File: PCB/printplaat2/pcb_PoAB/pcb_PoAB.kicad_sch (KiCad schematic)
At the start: 28 parts, among them J1 battertij, J2 lichtmeter1, J3 lichtmeter2, J4 lichtmeter3, J5 lichtmeter4, J6 lamp1, J7 lamp2, J8 lamp3, J9 spannigsmeter, U1 L7805CV, U2 AQY211EHAZ, U3 AQY211EHAZ, U4 AQY211EHAZ, U5 ACS712ELCTR-05B-T, U6 ACS712ELCTR-05B-T, U7 ACS712ELCTR-05B-T, U9 ARDUINO_MKR_WAN_1310

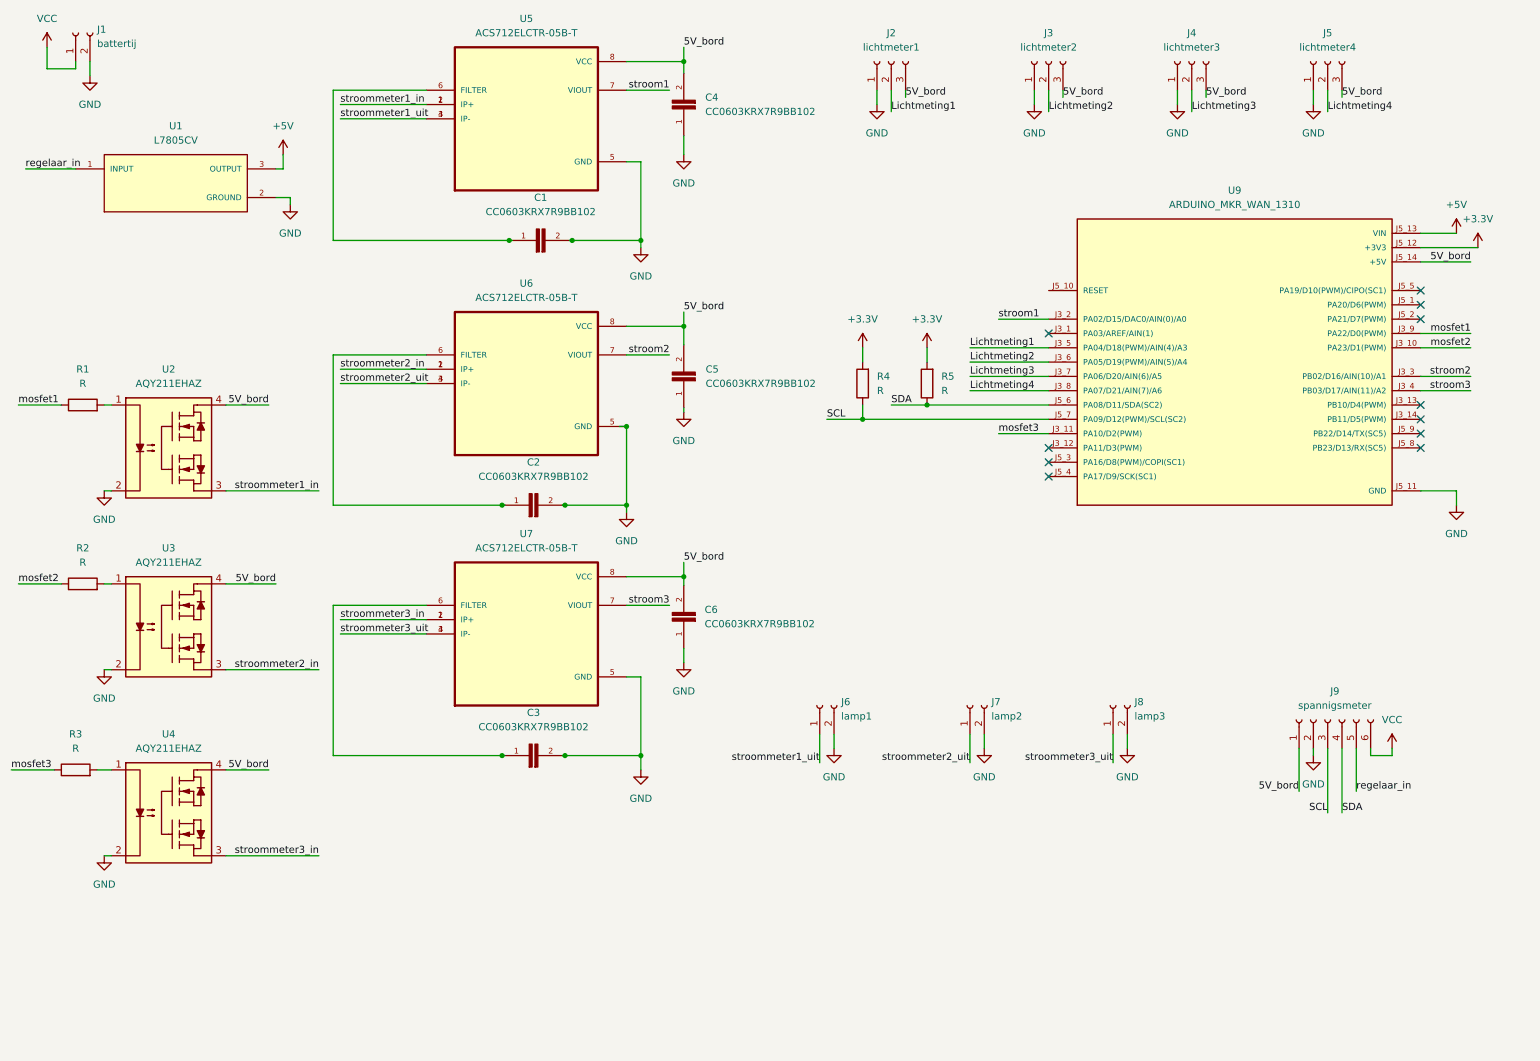
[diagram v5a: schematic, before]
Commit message: PCB en schema spanning en stroommetingen aangepast
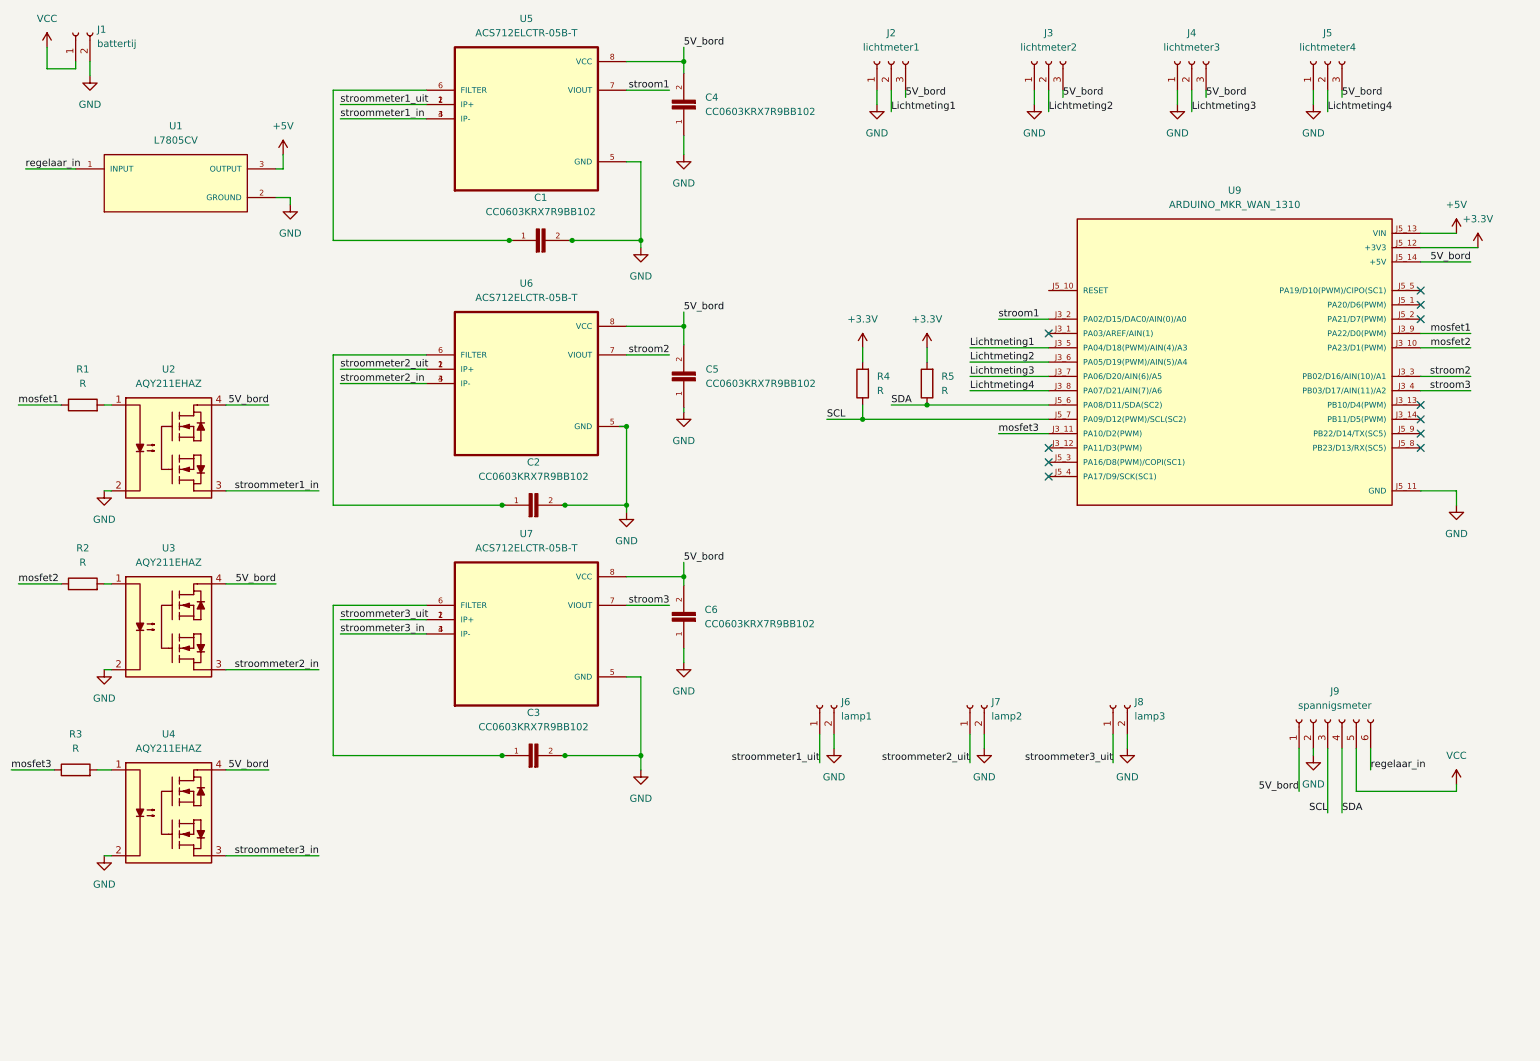
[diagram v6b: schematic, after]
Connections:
- net VCC: now also J9.5 (Pin_5); no longer J9.6 (Pin_6)
- net regelaar_in: now also J9.6 (Pin_6); no longer J9.5 (Pin_5)
- net stroommeter1_in: now also U5.3 (IP-), U5.4 (IP-); no longer U5.1 (IP+), U5.2 (IP+)
- net stroommeter1_uit: now also U5.1 (IP+), U5.2 (IP+); no longer U5.3 (IP-), U5.4 (IP-)
- net stroommeter2_in: now also U6.3 (IP-), U6.4 (IP-); no longer U6.1 (IP+), U6.2 (IP+)
- net stroommeter2_uit: now also U6.1 (IP+), U6.2 (IP+); no longer U6.3 (IP-), U6.4 (IP-)
- net stroommeter3_in: now also U7.3 (IP-), U7.4 (IP-); no longer U7.1 (IP+), U7.2 (IP+)
- net stroommeter3_uit: now also U7.1 (IP+), U7.2 (IP+); no longer U7.3 (IP-), U7.4 (IP-)
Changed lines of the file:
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@@
     (stroke (width 0) (type default) (color 0 0 0 0))
   )
-  (wire (pts (xy 255.27 144.78) (xy 255.27 143.51))
+  (wire (pts (xy 255.27 147.32) (xy 255.27 143.51))
     (stroke (width 0) (type default) (color 0 0 0 0))
   )
@@
     (stroke (width 0) (type default) (color 0 0 0 0))
   )
-  (wire (pts (xy 259.08 143.51) (xy 259.08 144.78))
+  (wire (pts (xy 252.73 151.13) (xy 270.51 151.13))
     (stroke (width 0) (type default) (color 0 0 0 0))
   )
@@
     (stroke (width 0) (type default) (color 0 0 0 0))
   )
+  (wire (pts (xy 270.51 151.13) (xy 270.51 149.86))
+    (stroke (width 0) (type default) (color 0 0 0 0))
+  )
   (wire (pts (xy 71.12 73.66) (xy 87.63 73.66))
     (stroke (width 0) (type default) (color 0 0 0 0))
   )
-  (wire (pts (xy 259.08 144.78) (xy 255.27 144.78))
-    (stroke (width 0) (type default) (color 0 0 0 0))
-  )
   (wire (pts (xy 13.97 147.32) (xy 21.59 147.32))
     (stroke (width 0) (type default) (color 0 0 0 0))
@@
     (stroke (width 0) (type default) (color 0 0 0 0))
   )
-  (label "stroommeter3_in" (at 72.39 120.65 0)
-    (effects (font (size 1.27 1.27)) (justify left bottom))
-  )
   (label "5V_bord" (at 226.06 27.94 0)
     (effects (font (size 1.27 1.27)) (justify left bottom))
@@
     (effects (font (size 1.27 1.27)) (justify right bottom))
   )
-  (label "stroommeter3_uit" (at 72.39 123.19 0)
-    (effects (font (size 1.27 1.27)) (justify left bottom))
-  )
   (label "Lichtmeting3" (at 184.15 77.47 0)
     (effects (font (size 1.27 1.27)) (justify left bottom))
@@
     (effects (font (size 1.27 1.27)) (justify left bottom))
   )
-  (label "stroommeter2_in" (at 72.39 76.2 0)
-    (effects (font (size 1.27 1.27)) (justify left bottom))
-  )
   (label "mosfet2" (at 15.24 114.3 0)
     (effects (font (size 1.27 1.27)) (justify left bottom))
@@
     (effects (font (size 1.27 1.27)) (justify right bottom))
   )
-  (label "stroommeter1_in" (at 72.39 29.21 0)
-    (effects (font (size 1.27 1.27)) (justify left bottom))
-  )
-  (label "regelaar_in" (at 252.73 151.13 0)
-    (effects (font (size 1.27 1.27)) (justify left bottom))
-  )
   (label "stroom3" (at 130.81 118.11 180)
     (effects (font (size 1.27 1.27)) (justify right bottom))
@@
     (effects (font (size 1.27 1.27)) (justify left bottom))
   )
-  (label "stroommeter2_uit" (at 72.39 78.74 0)
-    (effects (font (size 1.27 1.27)) (justify left bottom))
-  )
   (label "5V_bord" (at 250.19 27.94 0)
     (effects (font (size 1.27 1.27)) (justify left bottom))
@@
     (effects (font (size 1.27 1.27)) (justify right bottom))
   )
-  (label "stroommeter1_uit" (at 72.39 31.75 0)
-    (effects (font (size 1.27 1.27)) (justify left bottom))
-  )
   (label "mosfet3" (at 13.97 147.32 0)
     (effects (font (size 1.27 1.27)) (justify left bottom))
@@
     (effects (font (size 1.27 1.27)) (justify left bottom))
   )
+  (label "stroommeter2_in" (at 72.39 78.74 0)
+    (effects (font (size 1.27 1.27)) (justify left bottom))
+  )
+  (label "regelaar_in" (at 255.27 147.32 0)
+    (effects (font (size 1.27 1.27)) (justify left bottom))
+  )
   (label "Lichtmeting2" (at 198.12 30.48 0)
     (effects (font (size 1.27 1.27)) (justify left bottom))
@@
     (effects (font (size 1.27 1.27)) (justify right bottom))
   )
+  (label "stroommeter3_in" (at 72.39 123.19 0)
+    (effects (font (size 1.27 1.27)) (justify left bottom))
+  )
   (label "stroommeter2_uit" (at 184.15 146.05 180)
     (effects (font (size 1.27 1.27)) (justify right bottom))
   )
+  (label "stroommeter1_in" (at 72.39 31.75 0)
+    (effects (font (size 1.27 1.27)) (justify left bottom))
+  )
   (label "mosfet2" (at 273.05 72.39 180)
     (effects (font (size 1.27 1.27)) (justify right bottom))
@@
     (effects (font (size 1.27 1.27)) (justify right bottom))
   )
+  (label "stroommeter1_uit" (at 72.39 29.21 0)
+    (effects (font (size 1.27 1.27)) (justify left bottom))
+  )
+  (label "stroommeter2_uit" (at 72.39 76.2 0)
+    (effects (font (size 1.27 1.27)) (justify left bottom))
+  )
   (label "Lichtmeting4" (at 184.15 80.01 0)
     (effects (font (size 1.27 1.27)) (justify left bottom))
   )
   (label "5V_bord" (at 200.66 27.94 0)
+    (effects (font (size 1.27 1.27)) (justify left bottom))
+  )
+  (label "stroommeter3_uit" (at 72.39 120.65 0)
     (effects (font (size 1.27 1.27)) (justify left bottom))
   )
@@
     )
     (property "Datasheet" "" (id 3) (at 30.48 129.54 0)
+      (effects (font (size 1.27 1.27)) hide)
+    )
+    (pin "1")
+  )
+  (symbol (lib_id "power:VCC") (at 270.51 149.86 0) (unit 1)
+    (in_bom yes) (on_board yes) (fields_autoplaced)
+    (property "Reference" "#PWR?" (id 0) (at 270.51 153.67 0)
+      (effects (font (size 1.27 1.27)) hide)
+    )
+    (property "Value" "VCC" (id 1) (at 270.51 144.78 0))
+    (property "Footprint" "" (id 2) (at 270.51 149.86 0)
+      (effects (font (size 1.27 1.27)) hide)
+    )
+    (property "Datasheet" "" (id 3) (at 270.51 149.86 0)
       (effects (font (size 1.27 1.27)) hide)
     )
@@
     (pin "2")
     (pin "3")
-  )
-  (symbol (lib_id "power:VCC") (at 259.08 143.51 0) (unit 1)
-    (in_bom yes) (on_board yes) (fields_autoplaced)
-    (property "Reference" "#PWR0104" (id 0) (at 259.08 147.32 0)
-      (effects (font (size 1.27 1.27)) hide)
-    )
-    (property "Value" "VCC" (id 1) (at 259.08 138.43 0))
-    (property "Footprint" "" (id 2) (at 259.08 143.51 0)
-      (effects (font (size 1.27 1.27)) hide)
-    )
-    (property "Datasheet" "" (id 3) (at 259.08 143.51 0)
-      (effects (font (size 1.27 1.27)) hide)
-    )
-    (pin "1")
   )
   (symbol (lib_id "CC0603KRX7R9BB102:CC0603KRX7R9BB102") (at 107.95 53.34 0) (unit 1)
@@
       (reference "#PWR0103") (unit 1) (value "+3.3V") (footprint "")
     )
-    (path "/69ebda95-083c-43f9-b0df-38d5ed933405"
-      (reference "#PWR0104") (unit 1) (value "VCC") (footprint "")
-    )
     (path "/3add1d4c-fb5a-440c-8930-b4d5cc6dbb8d"
       (reference "#PWR0105") (unit 1) (value "+3.3V") (footprint "")
@@
       (reference "#PWR0106") (unit 1) (value "+5V") (footprint "")
     )
+    (path "/15b33a27-1da1-4eb8-82f7-f31d9459254e"
+      (reference "#PWR?") (unit 1) (value "VCC") (footprint "")
+    )
     (path "/6fbca105-5745-401d-ba3b-74158c957239"

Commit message: stroometingen en zips
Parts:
- added J?: GPS, symbol Connector:Conn_01x04_Female
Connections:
- net 5V_bord: now also J?.1 (Pin_1)
- net GND: now also J?.4 (Pin_4)
- net TX: now reaches U9.J5_8 (PB23/D13/RX(SC5))
- net TX: now also J?.3 (Pin_3)
- net RX: now reaches U9.J5_9 (PB22/D14/TX(SC5))
- net RX: now also J?.2 (Pin_2)
- no-connect marks 11 -> 9
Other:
- moved on the sheet: J6, J7, J8, J9

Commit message: schema baseplate aangepast
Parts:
- added C7, C8: C, Capacitor_SMD:C_0805_2012Metric_Pad1.18x1.45mm_HandSolder, symbol Device:C
- added R6, R7: R, Resistor_SMD:R_0805_2012Metric_Pad1.20x1.40mm_HandSolder, symbol Device:R
- added U8: ADS1115, ADS1115:MSOP10, symbol ADS1115:ADS1115
- J10: renamed from J?; footprint (none) -> Connector_PinSocket_2.54mm:PinSocket_1x04_P2.54mm_Vertical
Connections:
- net 5V_bord: now also C7.1, C8.1, R6.2, U8.8; no longer U2.4 (VCC), U3.4 (VCC), U4.4 (VCC)
- net GND: now also C7.2, C8.2, R7.1, U8.3
- net SCL: now also U8.10
- net SDA: now also U8.9
- net VCC: now also U2.4 (VCC), U3.4 (VCC), U4.4 (VCC)
- net stroom1: now also U8.4; no longer U9.J3_2 (PA02/D15/DAC0/AIN(0)/A0)
- net stroom2: now also U8.5; no longer U9.J3_3 (PB02/D16/AIN(10)/A1)
- net stroom3: now also U8.6; no longer U9.J3_4 (PB03/D17/AIN(11)/A2)
- new net: R7.2, U8.1
- new net: R6.1, U8.2
- no-connect marks 9 -> 13
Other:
- moved on the sheet: J10, J6, J7, J8, J9
